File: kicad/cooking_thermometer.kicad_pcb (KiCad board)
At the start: 2 copper layers, 88.9 x 50.8 mm, 36 parts, among them J1 FTDI, J2 STLINK, J3 3V3_Power, J4 Battery, J6 OLED_CONN, J7 USB_B_Micro, J8 THERMO_CONN, SW1 BOOT0_SW, SW2 NRST_SW, SW3 UI_A_SW, SW4 UI_B_SW, SW5 UI_C_SW, U1 STM32F070F6Px, U2 MCP1700x-330xxTO, U3 MCP73831-2-OT

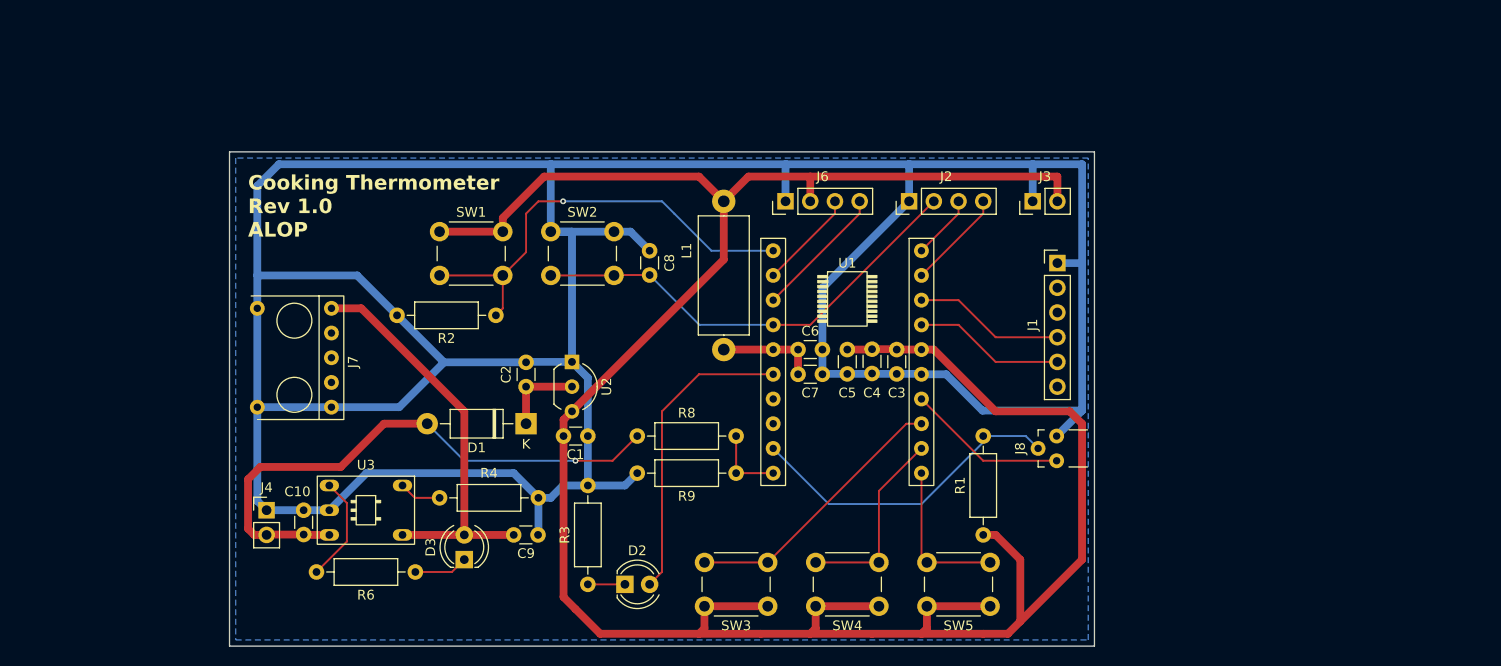
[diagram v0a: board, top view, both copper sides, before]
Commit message: Add passive buzzer to schematic, layout, stm32cube
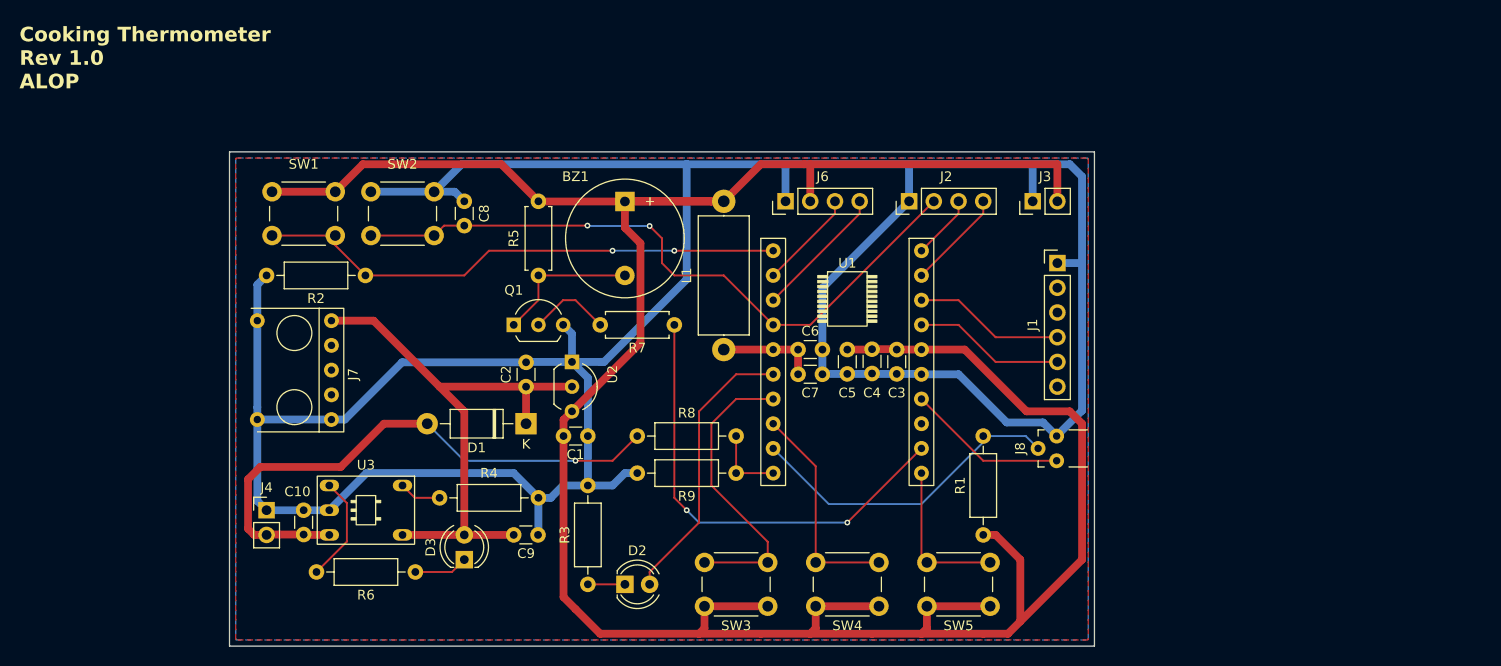
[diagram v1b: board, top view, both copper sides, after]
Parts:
- added BZ1: Passive_Buzzer, Buzzer_Beeper:Buzzer_12x9.5RM7.6, F.Cu at (134.6, 85.1)
- added Q1: BC547, Package_TO_SOT_THT:TO-92L_Inline_Wide, F.Cu at (123.2, 97.8)
- added R5: 1k, Resistor_THT:R_Axial_DIN0207_L6.3mm_D2.5mm_P7.62mm_Horizontal, F.Cu at (125.7, 85.1)
- added R7: 4k7, Resistor_THT:R_Axial_DIN0207_L6.3mm_D2.5mm_P7.62mm_Horizontal, F.Cu at (139.7, 97.8)
- moved C8 19.7 mm to (118.1, 85.1)
- moved SW2 18.9 mm to (108.5, 84.1)
- moved SW1 17.7 mm to (98.3, 84.1)
- moved R2 14.0 mm to (108.0, 92.7)
- moved J7 1.27 mm to (104.5, 110.1)
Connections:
- C2 pad 1: 5V -> +5V_USB
- D1 pad 1: 5V -> +5V_USB
- U1 pad 12: /UI_B -> /TIM3_CH1_BUZZER_PWM
- U1 pad 13: /UI_A -> unconnected-(U1-PA7-Pad13)
- U1 pad 7: unconnected-(U1-PA1-Pad7) -> /UI_A
- U1 pad 8: unconnected-(U1-PA2-Pad8) -> /UI_B
- U2 pad 2: 5V -> +5V_USB
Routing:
- net /TIM3_CH1_BUZZER_PWM: track 0.00 -> 47.4 mm, vias 0 -> 2
- net GND: track 361.8 -> 318.3 mm
- net +3.3V: track 260.6 -> 286.7 mm
- net /NRST: track 46.8 -> 69.3 mm, vias 0 -> 2
- net +5V_USB: track 42.2 -> 59.1 mm
- net Net-(BZ1--): track 0.00 -> 15.0 mm
- net Net-(U1-BOOT0): track 46.3 -> 54.8 mm, vias 1 -> 2
- net 5V: track 8.53 -> 0.00 mm
- net Net-(Q1-B): track 0.00 -> 8.45 mm
- net /UI_B: track 20.0 -> 22.6 mm
- net /UI_A: track 28.2 -> 30.6 mm
- net /UI_LED: track 31.3 -> 29.1 mm
- added copper zone on F.Cu, net GND

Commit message: Rearrange signals to better fit board
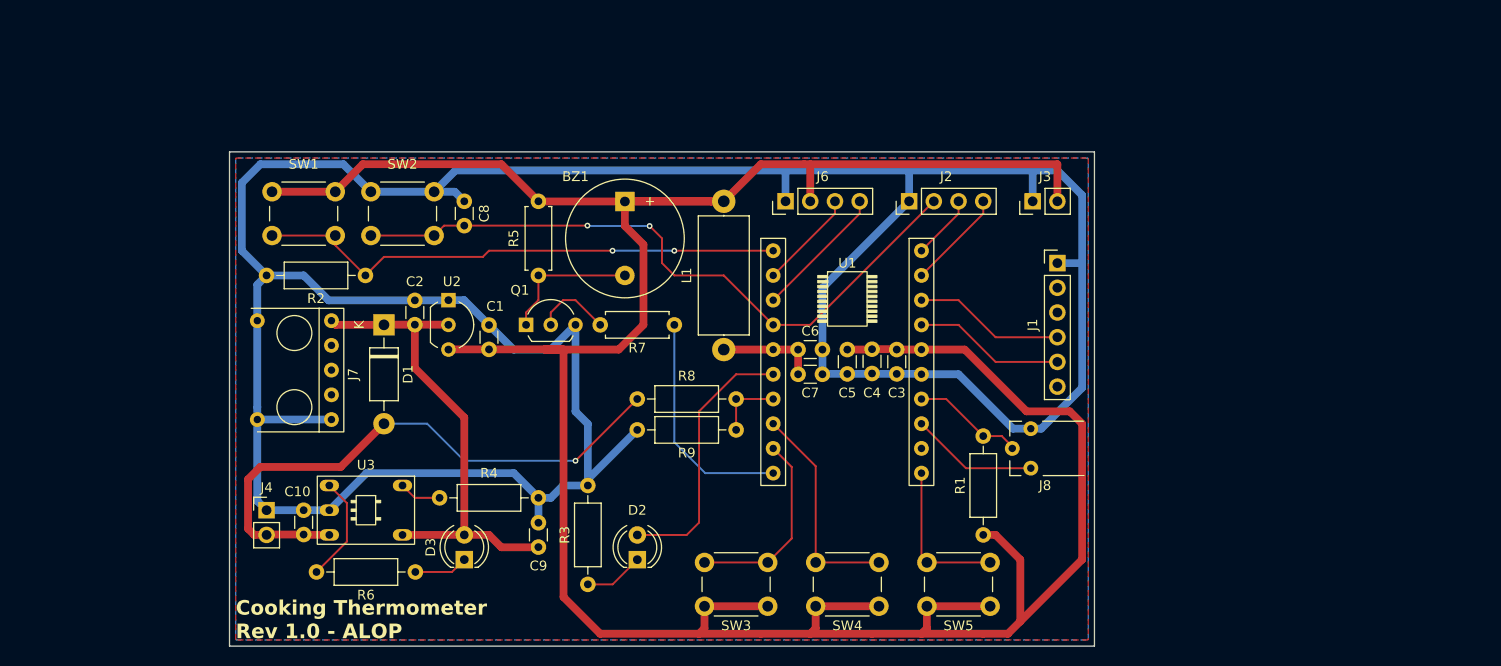
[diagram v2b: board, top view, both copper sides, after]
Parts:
- moved D1 17.8 mm to (109.9, 97.8), turned to -90 degrees
- moved U2 14.2 mm to (116.5, 95.2)
- moved C2 13.1 mm to (113.0, 97.8)
- moved C1 11.8 mm to (120.7, 100.3), turned to 90 degrees
- moved J8 7.10 mm to (174.4, 113.0)
- moved R9 4.45 mm to (146.1, 108.6)
- moved R8 3.81 mm to (135.9, 105.4)
- moved D2 2.84 mm to (135.9, 121.9), turned to 90 degrees
- moved C9 2.83 mm to (125.7, 120.6), turned to 90 degrees
- moved Q1 1.27 mm to (124.5, 97.8)
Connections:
- J8 pad S: /ADC_IN3 -> /ADC9_TEMP_MEAS
- R1 pad 2: /ADC_IN3 -> /ADC9_TEMP_MEAS
- R7 pad 1: /TIM3_CH1_BUZZER_PWM -> /TIM14_CH1_BUZZER_PWM
- R8 pad 2: /ADC_IN4 -> /ADC1_BATT_MEAS
- R9 pad 1: /ADC_IN4 -> /ADC1_BATT_MEAS
- U1 pad 10: /ADC_IN4 -> /TIM14_CH1_BUZZER_PWM
- U1 pad 12: /TIM3_CH1_BUZZER_PWM -> unconnected-(U1-PA6-Pad12)
- U1 pad 13: unconnected-(U1-PA7-Pad13) -> /~{JACK_CONNECTED}
- U1 pad 14: /~{JACK_CONNECTED} -> /ADC9_TEMP_MEAS
- U1 pad 7: /UI_A -> /ADC1_BATT_MEAS
- U1 pad 9: /ADC_IN3 -> /UI_A
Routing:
- net /TIM3_CH1_BUZZER_PWM: track 47.4 -> 0.00 mm, vias 2 -> 0
- net /ADC_IN3: track 33.4 -> 0.00 mm
- net /TIM14_CH1_BUZZER_PWM: track 0.00 -> 23.5 mm
- net +3.3V: track 286.7 -> 305.9 mm
- net /ADC9_TEMP_MEAS: track 0.00 -> 11.6 mm
- net /UI_A: track 30.6 -> 20.0 mm
- net +5V_USB: track 59.1 -> 50.4 mm
- net /ADC_IN4: track 7.62 -> 0.00 mm
- net /ADC1_BATT_MEAS: track 0.00 -> 6.98 mm
- net /~{JACK_CONNECTED}: track 16.5 -> 13.1 mm
- net GND: track 318.3 -> 320.6 mm
- net Net-(D2-K): track 3.81 -> 6.14 mm
- net /UI_LED: track 29.1 -> 27.5 mm
- net +BATT: track 58.7 -> 60.3 mm
- net Net-(Q1-B): track 8.45 -> 7.93 mm
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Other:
- board text added: "Cooking Thermometer Rev 1.0 - ALOP"
- board text removed: "Cooking Thermometer Rev 1.0 ALOP"

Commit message: Change schematic/layout to stm32g0b0ke (LQFP32)
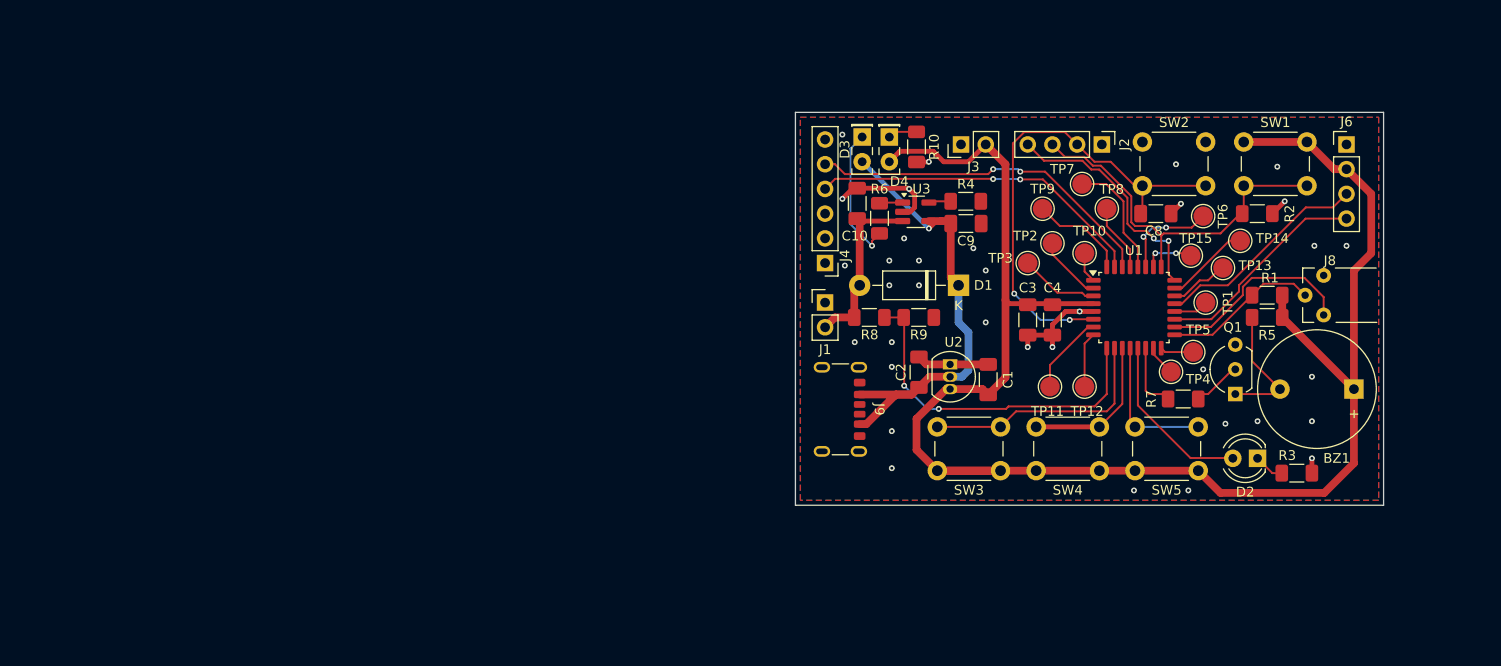
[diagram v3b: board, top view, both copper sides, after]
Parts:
- removed C5: 100nF, Capacitor_THT:C_Disc_D3.0mm_W1.6mm_P2.50mm
- removed C6: 1uF, Capacitor_THT:C_Disc_D3.0mm_W1.6mm_P2.50mm
- removed C7: 10nF, Capacitor_THT:C_Disc_D3.0mm_W1.6mm_P2.50mm
- removed J7: USB_B_Micro, MyOwnFootprintLibrary:uUSB-B_2.54mm_connector
- removed L1: 680nH, Inductor_THT:L_Axial_L12.0mm_D5.0mm_P15.24mm_Horizontal_Fastron_MISC
- added D4: GREEN_LED_PWR, LED_THT:LED_Rectangular_W5.0mm_H2.0mm, F.Cu at (161.8, 78.5)
- added J9: USB_C, Connector_USB:USB_C_Receptacle_GCT_USB4125-xx-x_6P_TopMnt_Horizontal, F.Cu at (155.7, 106.5)
- added R10: 330, Resistor_SMD:R_1206_3216Metric_Pad1.30x1.75mm_HandSolder, F.Cu at (164.6, 79.5)
- added TP1: PC6, TestPoint:TestPoint_Pad_D2.0mm, F.Cu at (194.3, 95.5)
- added TP10: PB9, TestPoint:TestPoint_Pad_D2.0mm, F.Cu at (181.9, 90.4)
- added TP11: PA0, TestPoint:TestPoint_Pad_D2.0mm, F.Cu at (178.3, 104.1)
- added TP12: PA1, TestPoint:TestPoint_Pad_D2.0mm, F.Cu at (181.9, 104.1)
- added TP13: PA11/9, TestPoint:TestPoint_Pad_D2.0mm, F.Cu at (196.1, 91.9)
- added TP14: PA12/10, TestPoint:TestPoint_Pad_D2.0mm, F.Cu at (197.9, 89.2)
- added TP15: PA15, TestPoint:TestPoint_Pad_D2.0mm, F.Cu at (192.8, 90.7)
- added TP2: PC14, TestPoint:TestPoint_Pad_D2.0mm, F.Cu at (178.6, 89.4)
- added TP3: PC15, TestPoint:TestPoint_Pad_D2.0mm, F.Cu at (176.0, 91.4)
- added TP4: PB0, TestPoint:TestPoint_Pad_D2.0mm, F.Cu at (190.8, 102.6)
- added TP5: PB1, TestPoint:TestPoint_Pad_D2.0mm, F.Cu at (193.0, 100.6)
- added TP6: PB3, TestPoint:TestPoint_Pad_D2.0mm, F.Cu at (194.1, 86.6)
- added TP7: PB4, TestPoint:TestPoint_Pad_D2.0mm, F.Cu at (181.6, 83.3)
- added TP8: PB5, TestPoint:TestPoint_Pad_D2.0mm, F.Cu at (184.2, 85.9)
- added TP9: PB8, TestPoint:TestPoint_Pad_D2.0mm, F.Cu at (177.5, 85.9)
- C1, C10, C2, C3, C4, C8, C9: footprint Capacitor_THT:C_Disc_D3.0mm_W1.6mm_P2.50mm -> Capacitor_SMD:C_1206_3216Metric_Pad1.33x1.80mm_HandSolder
- D3: footprint LED_THT:LED_D4.0mm -> LED_THT:LED_Rectangular_W5.0mm_H2.0mm
- R1, R2, R3, R4, R6, R8, R9: footprint Resistor_THT:R_Axial_DIN0207_L6.3mm_D2.5mm_P10.16mm_Horizontal -> Resistor_SMD:R_1206_3216Metric_Pad1.30x1.75mm_HandSolder
- R5, R7: footprint Resistor_THT:R_Axial_DIN0207_L6.3mm_D2.5mm_P7.62mm_Horizontal -> Resistor_SMD:R_1206_3216Metric_Pad1.30x1.75mm_HandSolder
- U1: value STM32F070F6Px -> STM32G0B0KETx; footprint MyOwnFootprintLibrary:STM32F070_DIP20 -> Package_QFP:LQFP-32_7x7mm_P0.8mm
- U2: footprint Package_TO_SOT_THT:TO-92_Inline_Wide -> Package_TO_SOT_THT:TO-92_Inline
- U3: footprint MyOwnFootprintLibrary:DIP-5-6_7.62mm_5on6 -> Package_TO_SOT_SMD:SOT-23-5_HandSoldering
- moved SW1 100.0 mm to (198.2, 79.0)
- moved R2 91.9 mm to (199.6, 86.4), turned to 0 degrees
- moved SW2 79.5 mm to (187.8, 79.0)
- moved BZ1 77.4 mm to (209.6, 104.4), turned to 180 degrees
- moved R5 75.8 mm to (200.6, 97.0), turned to 180 degrees
- moved R3 73.8 mm to (203.7, 113.0), turned to 0 degrees
- moved Q1 73.2 mm to (197.4, 104.9), turned to 90 degrees
- moved C8 71.1 mm to (189.2, 86.4), turned to 180 degrees
- moved C10 66.3 mm to (158.5, 85.3)
- moved D2 64.6 mm to (199.6, 111.5), turned to 180 degrees
- moved U3 64.3 mm to (164.5, 86.2), turned to 0 degrees
- moved J4 61.2 mm to (155.2, 95.5)
- moved R6 60.0 mm to (160.8, 86.8), turned to 90 degrees
- moved D3 59.7 mm to (159.0, 78.5), turned to -90 degrees
- moved D1 59.2 mm to (168.9, 93.7), turned to 180 degrees
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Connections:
- J2 pad 3: /SWCLK -> /BOOT0
- J8 pad S: /ADC9_TEMP_MEAS -> /ADC10_TEMP_MEAS
- R1 pad 2: /ADC9_TEMP_MEAS -> /ADC10_TEMP_MEAS
- R2 pad 1: Net-(U1-BOOT0) -> /BOOT0
- R7 pad 1: /TIM14_CH1_BUZZER_PWM -> /TIM3_CH2_BUZZER_PWM
- R8 pad 2: /ADC1_BATT_MEAS -> /ADC2_BATT_MEAS
- R9 pad 1: /ADC1_BATT_MEAS -> /ADC2_BATT_MEAS
- SW1 pad 2: Net-(U1-BOOT0) -> /BOOT0
- U1 pad 1: Net-(U1-BOOT0) -> Net-(U1-PB9)
- U1 pad 10: /TIM14_CH1_BUZZER_PWM -> /UI_A
- U1 pad 11: /UI_C -> /UI_B
- U1 pad 12: unconnected-(U1-PA6-Pad12) -> /UI_C
- U1 pad 13: /~{JACK_CONNECTED} -> /UI_LED
- U1 pad 14: /ADC9_TEMP_MEAS -> /TIM3_CH2_BUZZER_PWM
- U1 pad 15: GND -> Net-(U1-PB0)
- U1 pad 16: +3.3V -> Net-(U1-PB1)
- U1 pad 17: /UART1_TX -> /ADC10_TEMP_MEAS
- U1 pad 18: /UART1 RX -> /~{JACK_CONNECTED}
- U1 pad 19: /SWDIO -> /I2C1_SCL
- U1 pad 2: /I2C1_SDA -> Net-(U1-PC14)
- U1 pad 20: /SWCLK -> Net-(U1-PC6)
- U1 pad 3: /I2C1_SCL -> Net-(U1-PC15)
- U1 pad 4: /NRST -> +3.3V
- U1 pad 5: Net-(U1-VDDA) -> GND
- U1 pad 6: /UI_LED -> /NRST
- U1 pad 7: /ADC1_BATT_MEAS -> Net-(U1-PA0)
- U1 pad 8: /UI_B -> Net-(U1-PA1)
- U1 pad 9: /UI_A -> /ADC2_BATT_MEAS
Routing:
- net GND: track 320.6 -> 35.2 mm, vias 0 -> 35
- net +3.3V: track 305.9 -> 171.1 mm
- net Net-(U1-BOOT0): track 54.8 -> 0.00 mm, vias 2 -> 0
- net +BATT: track 60.3 -> 18.3 mm, vias 1 -> 0
- net /BOOT0: track 0.00 -> 38.4 mm
- net /ADC2_BATT_MEAS: track 0.00 -> 36.2 mm, vias 0 -> 2
- net /TIM14_CH1_BUZZER_PWM: track 23.5 -> 0.00 mm
- net /UART1_TX: track 15.5 -> 36.4 mm, vias 0 -> 2
- net /UART1 RX: track 15.5 -> 34.9 mm, vias 0 -> 2
- net /NRST: track 69.3 -> 50.3 mm
- net /ADC10_TEMP_MEAS: track 0.00 -> 16.1 mm
- net /SWDIO: track 10.3 -> 24.5 mm, vias 0 -> 2
- net Net-(U1-PB4): track 0.00 -> 12.4 mm
- net /I2C1_SDA: track 10.3 -> 22.3 mm
- net /ADC9_TEMP_MEAS: track 11.6 -> 0.00 mm
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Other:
- board size 88.9 x 50.8 mm -> 60.5 x 40.4 mm
- board text removed: "Cooking Thermometer Rev 1.0 - ALOP"

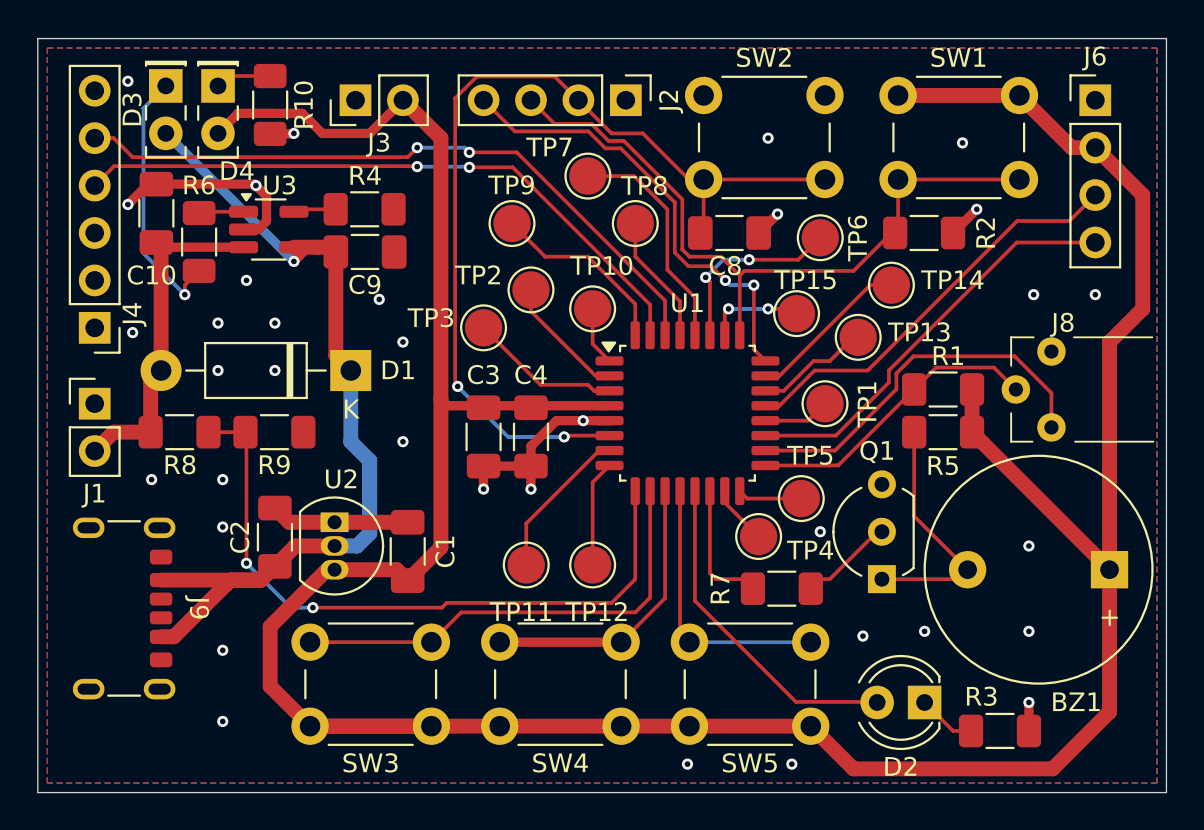
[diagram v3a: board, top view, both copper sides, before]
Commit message: Change to longer pads and some other adjustments
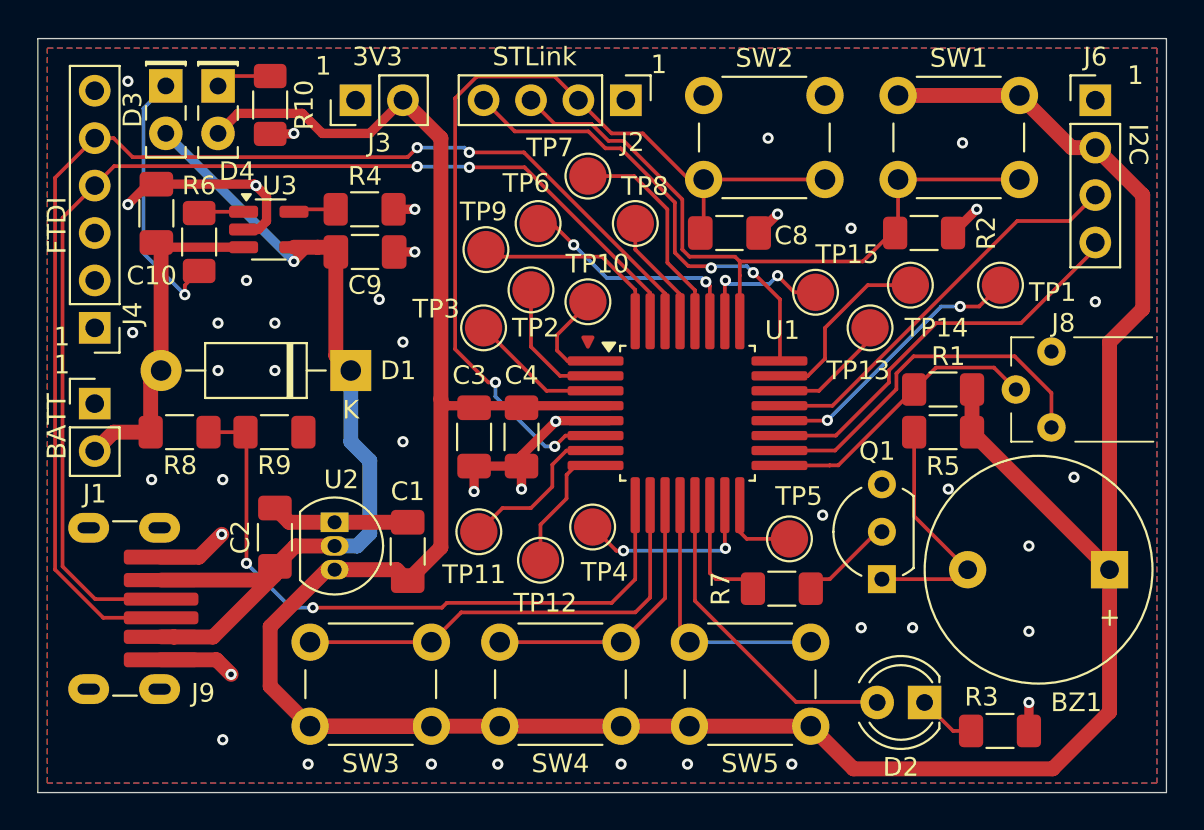
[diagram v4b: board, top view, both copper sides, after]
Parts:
- J9: footprint Connector_USB:USB_C_Receptacle_GCT_USB4125-xx-x_6P_TopMnt_Horizontal -> MyOwnFootprintLibrary:USB_C_Receptacle_GCT_USB4125-xx-x_6P_TopMnt_Horizontal_Long_Pads
- U1: footprint Package_QFP:LQFP-32_7x7mm_P0.8mm -> MyOwnFootprintLibrary:LQFP-32_7x7mm_P0.8mm_Long_pads
- moved TP6 15.1 mm to (178.9, 85.9)
- moved TP1 11.3 mm to (203.7, 89.2)
- moved TP4 8.90 mm to (181.9, 102.1)
- moved TP11 3.10 mm to (175.8, 102.4)
- moved TP12 2.81 mm to (179.1, 103.9)
- moved TP5 2.25 mm to (192.4, 102.7)
- moved TP9 1.98 mm to (176.1, 87.2)
- moved TP15 1.53 mm to (193.8, 89.5)
- moved TP14 1.02 mm to (198.9, 89.2)
- moved TP13 0.81 mm to (196.7, 91.4)
- moved C4 0.51 mm to (178.1, 97.3)
- moved C3 0.51 mm to (175.5, 97.3)
- moved TP10 0.46 mm to (181.6, 90.0)
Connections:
- J9 pad A5: unconnected-(J9-CC1-PadA5) -> /UART1 RX
- J9 pad B5: unconnected-(J9-CC2-PadB5) -> /UART1_TX
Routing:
- net /UART1_TX: track 36.4 -> 67.4 mm
- net /UART1 RX: track 34.9 -> 62.4 mm
- net Net-(U1-PC6): track 3.57 -> 14.8 mm, vias 0 -> 2
- net GND: track 35.2 -> 45.6 mm, vias 35 -> 43
- net Net-(U1-PB0): track 3.18 -> 10.0 mm, vias 0 -> 2
- net Net-(U1-PB9): track 3.16 -> 5.61 mm
- net Net-(U1-PA15): track 5.24 -> 7.65 mm
- net Net-(U1-PB3): track 10.2 -> 12.5 mm
- net Net-(U1-PA11/PA9): track 5.90 -> 7.37 mm
- net +5V_USB: track 48.4 -> 49.7 mm
- net Net-(U1-PB8): track 10.1 -> 11.3 mm
- net Net-(U1-PA12/PA10): track 8.76 -> 9.99 mm
- net Net-(U1-PA1): track 5.70 -> 6.92 mm
- net Net-(U1-PC14): track 6.79 -> 7.90 mm
- net Net-(U1-PB1): track 3.46 -> 4.25 mm
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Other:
- board text added: "1"
- board text added: "3V3"
- board text added: "BATT"
- board text added: "FTDI"
- board text added: "I2C"
- board text added: "STLink"
